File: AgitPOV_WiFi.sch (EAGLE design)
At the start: 42 parts

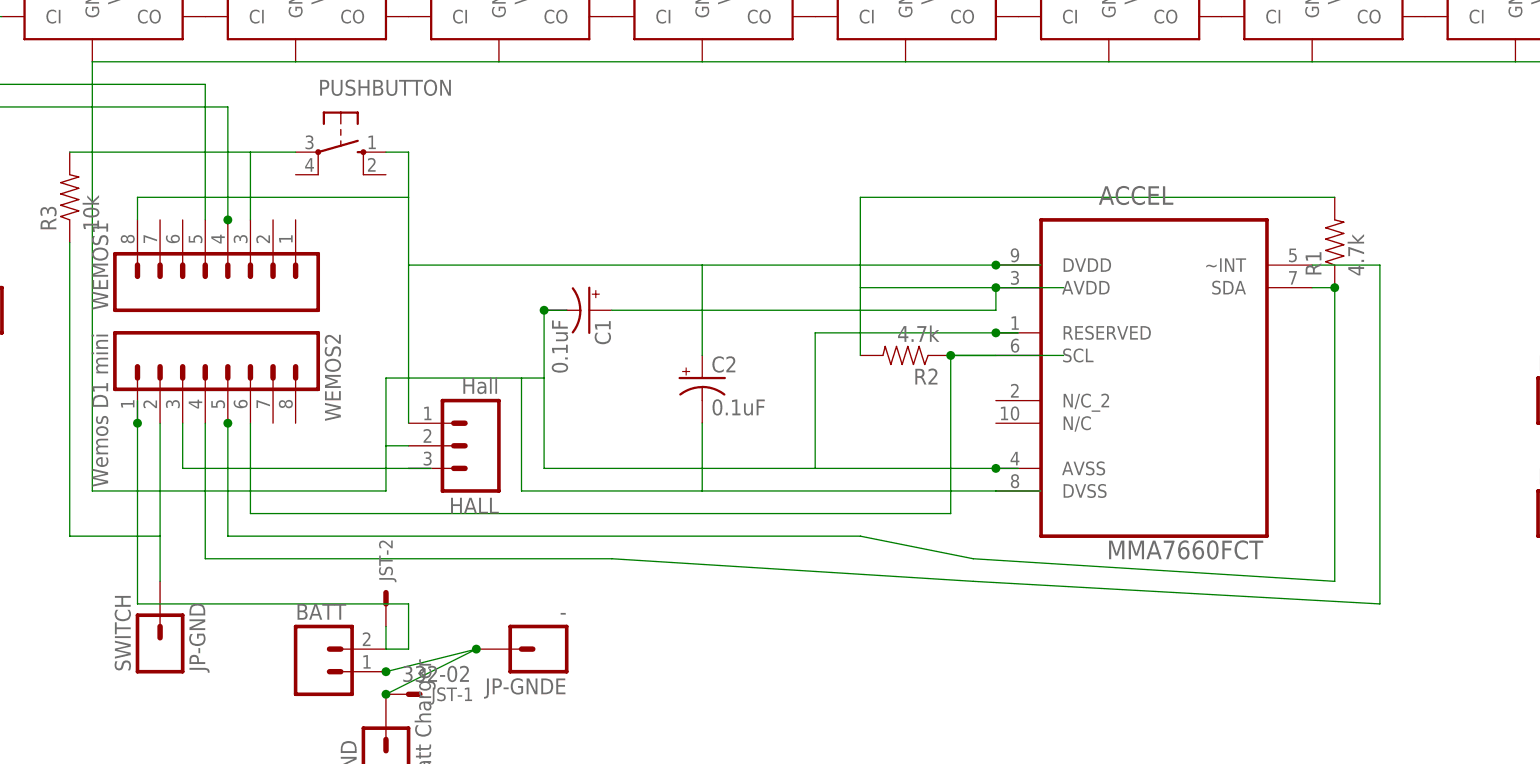
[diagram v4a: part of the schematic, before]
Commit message: Changed the interrupt pin from D3 to D7
D3 (and D4) when pulled to GND will prevent the Wemos from booting :/.
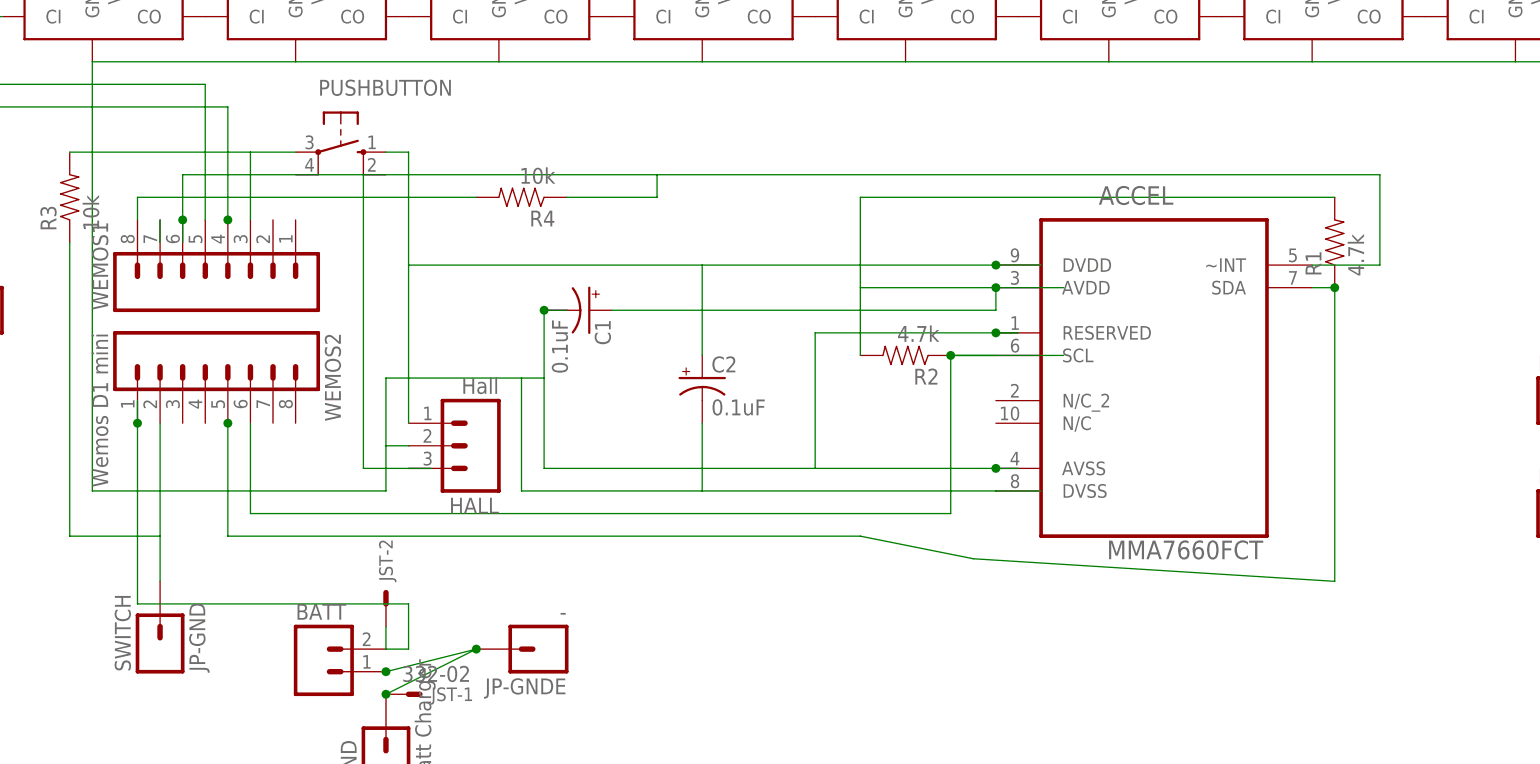
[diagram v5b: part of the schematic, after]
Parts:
- added R4: 10k, SparkFun-Resistors:RESISTOR1206
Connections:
- net N$5 renamed SCL
- net N$65 renamed SDA
- removed net N$67: ACCEL.~INT, WEMOS2.4
- new net INT: ACCEL.~INT, HALL.3, R4.1, WEMOS1.6
- net +3.3V: now also R4.2
- net N$1: now also WEMOS1.7; no longer HALL.3, WEMOS2.3
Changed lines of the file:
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@@
 <part name="R3" library="SparkFun-Resistors" deviceset="RESISTOR" device="1206" value="10k"/>
 <part name="C2" library="SparkFun-Capacitors" deviceset="10UF-16V-10%(TANT)" device="" value="0.1uF"/>
+<part name="R4" library="SparkFun-Resistors" deviceset="RESISTOR" device="1206" value="10k"/>
 </parts>
 <sheets>
@@
 <instance part="R3" gate="G$1" x="25.4" y="60.96" rot="R90"/>
 <instance part="C2" gate="G$1" x="96.52" y="40.64"/>
+<instance part="R4" gate="G$1" x="76.2" y="60.96" rot="R180"/>
 </instances>
 <busses>
@@
 <wire x1="96.52" y1="43.18" x2="96.52" y2="53.34" width="0.1524" layer="91"/>
 <pinref part="C2" gate="G$1" pin="+"/>
+<wire x1="63.5" y1="60.96" x2="71.12" y2="60.96" width="0.1524" layer="91"/>
+<pinref part="R4" gate="G$1" pin="2"/>
 </segment>
 </net>
@@
 </segment>
 </net>
-<net name="N$1" class="0">
-<segment>
-<pinref part="HALL" gate="G$1" pin="3"/>
-<wire x1="63.5" y1="30.48" x2="66.04" y2="30.48" width="0.1524" layer="91"/>
-<wire x1="63.5" y1="30.48" x2="38.1" y2="30.48" width="0.1524" layer="91"/>
-<wire x1="38.1" y1="30.48" x2="38.1" y2="35.56" width="0.1524" layer="91"/>
-<pinref part="WEMOS2" gate="G$1" pin="3"/>
-</segment>
-</net>
-<net name="N$5" class="0">
+<net name="SCL" class="0">
 <segment>
 <wire x1="137.16" y1="43.18" x2="124.46" y2="43.18" width="0.1524" layer="91"/>
@@
 </segment>
 </net>
-<net name="N$65" class="0">
+<net name="SDA" class="0">
 <segment>
 <wire x1="43.18" y1="35.56" x2="43.18" y2="22.86" width="0.1524" layer="91"/>
@@
 </segment>
 </net>
-<net name="N$67" class="0">
+<net name="INT" class="0">
 <segment>
 <wire x1="165.1" y1="53.34" x2="172.72" y2="53.34" width="0.1524" layer="91"/>
-<wire x1="172.72" y1="53.34" x2="172.72" y2="15.24" width="0.1524" layer="91"/>
-<wire x1="172.72" y1="15.24" x2="127" y2="17.78" width="0.1524" layer="91"/>
-<wire x1="127" y1="17.78" x2="86.36" y2="20.32" width="0.1524" layer="91"/>
-<wire x1="86.36" y1="20.32" x2="40.64" y2="20.32" width="0.1524" layer="91"/>
-<wire x1="40.64" y1="20.32" x2="40.64" y2="35.56" width="0.1524" layer="91"/>
-<pinref part="WEMOS2" gate="G$1" pin="4"/>
 <pinref part="ACCEL" gate="A" pin="~INT"/>
+<wire x1="38.1" y1="63.5" x2="58.42" y2="63.5" width="0.1524" layer="91"/>
+<wire x1="58.42" y1="63.5" x2="91.44" y2="63.5" width="0.1524" layer="91"/>
+<wire x1="91.44" y1="63.5" x2="172.72" y2="63.5" width="0.1524" layer="91"/>
+<wire x1="172.72" y1="63.5" x2="172.72" y2="53.34" width="0.1524" layer="91"/>
+<pinref part="HALL" gate="G$1" pin="3"/>
+<wire x1="63.5" y1="30.48" x2="66.04" y2="30.48" width="0.1524" layer="91"/>
+<wire x1="63.5" y1="30.48" x2="58.42" y2="30.48" width="0.1524" layer="91"/>
+<wire x1="58.42" y1="30.48" x2="58.42" y2="63.5" width="0.1524" layer="91"/>
+<pinref part="R4" gate="G$1" pin="1"/>
+<wire x1="81.28" y1="60.96" x2="91.44" y2="60.96" width="0.1524" layer="91"/>
+<wire x1="91.44" y1="60.96" x2="91.44" y2="63.5" width="0.1524" layer="91"/>
+<wire x1="38.1" y1="63.5" x2="38.1" y2="58.42" width="0.1524" layer="91"/>
+<pinref part="WEMOS1" gate="G$1" pin="6"/>
+<wire x1="38.1" y1="58.42" x2="38.1" y2="55.88" width="0.1524" layer="91"/>
+<junction x="38.1" y="58.42"/>
 </segment>
 </net>
@@
 </segment>
 </net>
+<net name="N$1" class="0">
+<segment>
+<pinref part="WEMOS1" gate="G$1" pin="7"/>
+<wire x1="35.56" y1="58.42" x2="35.56" y2="55.88" width="0.1524" layer="91"/>
+</segment>
+</net>

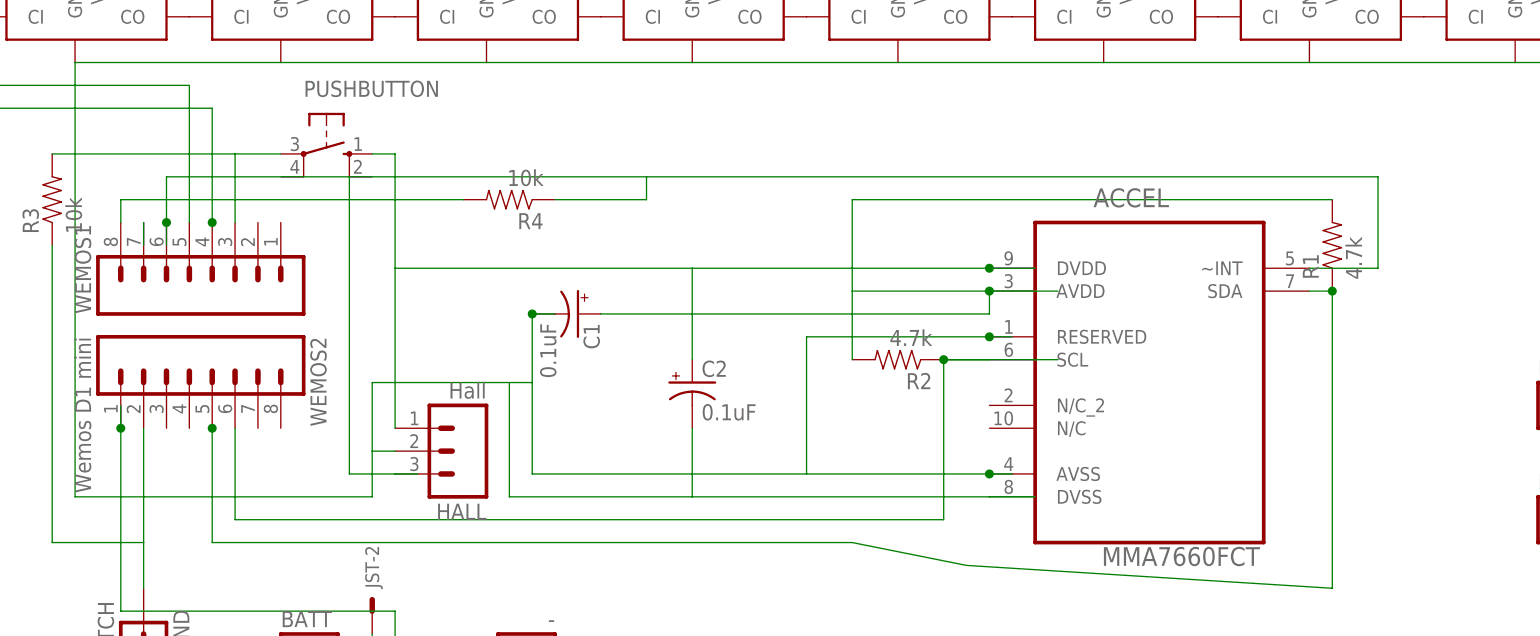
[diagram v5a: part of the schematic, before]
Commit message: Sin interrupt para el ACCEL! De regresar al sensor Hall en D4.
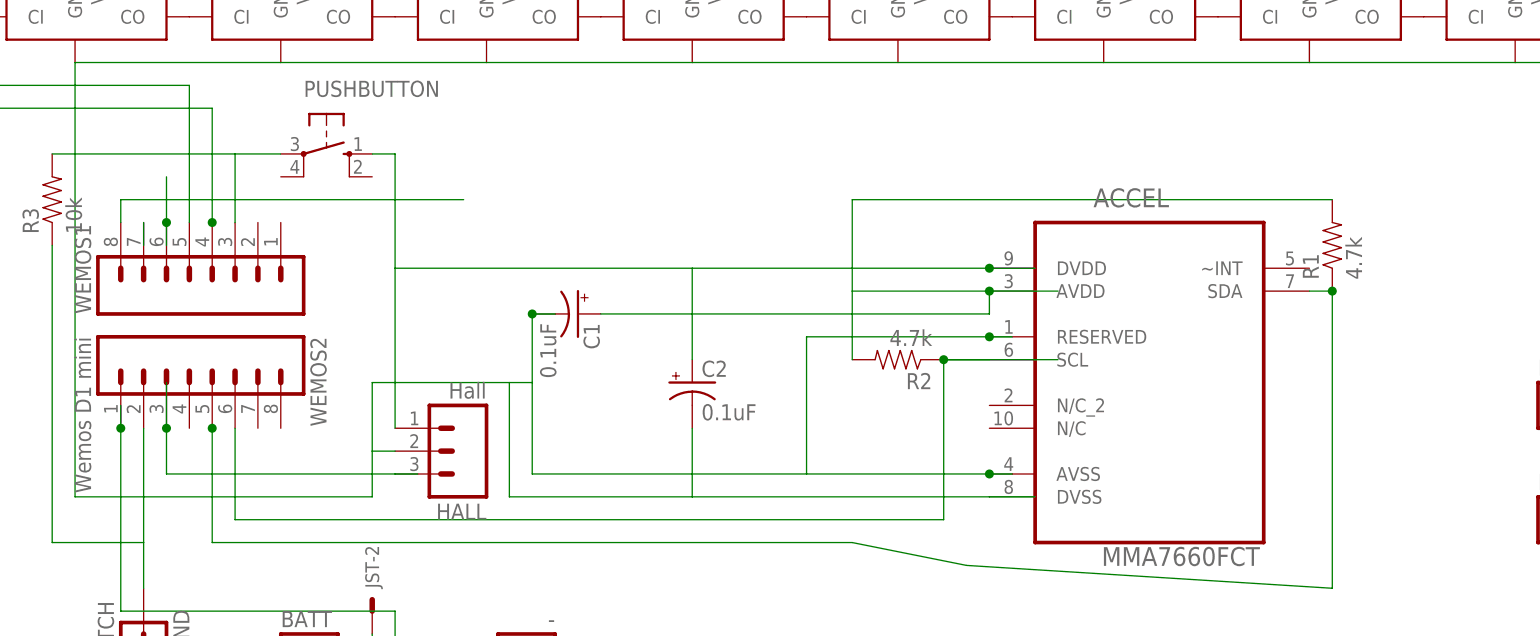
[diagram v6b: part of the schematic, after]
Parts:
- removed R4: 10k, SparkFun-Resistors:RESISTOR1206
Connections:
- removed net INT: ACCEL.~INT, HALL.3, R4.1, WEMOS1.6
- new net N$41: HALL.3, WEMOS2.3
- new net N$65: WEMOS1.6
- net +3.3V: no longer R4.2
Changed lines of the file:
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@@
 <part name="R3" library="SparkFun-Resistors" deviceset="RESISTOR" device="1206" value="10k"/>
 <part name="C2" library="SparkFun-Capacitors" deviceset="10UF-16V-10%(TANT)" device="" value="0.1uF"/>
-<part name="R4" library="SparkFun-Resistors" deviceset="RESISTOR" device="1206" value="10k"/>
 </parts>
 <sheets>
@@
 <instance part="R3" gate="G$1" x="25.4" y="60.96" rot="R90"/>
 <instance part="C2" gate="G$1" x="96.52" y="40.64"/>
-<instance part="R4" gate="G$1" x="76.2" y="60.96" rot="R180"/>
 </instances>
 <busses>
@@
 <pinref part="C2" gate="G$1" pin="+"/>
 <wire x1="63.5" y1="60.96" x2="71.12" y2="60.96" width="0.1524" layer="91"/>
-<pinref part="R4" gate="G$1" pin="2"/>
 </segment>
 </net>
@@
 </segment>
 </net>
-<net name="INT" class="0">
-<segment>
-<wire x1="165.1" y1="53.34" x2="172.72" y2="53.34" width="0.1524" layer="91"/>
-<pinref part="ACCEL" gate="A" pin="~INT"/>
-<wire x1="38.1" y1="63.5" x2="58.42" y2="63.5" width="0.1524" layer="91"/>
-<wire x1="58.42" y1="63.5" x2="91.44" y2="63.5" width="0.1524" layer="91"/>
-<wire x1="91.44" y1="63.5" x2="172.72" y2="63.5" width="0.1524" layer="91"/>
-<wire x1="172.72" y1="63.5" x2="172.72" y2="53.34" width="0.1524" layer="91"/>
-<pinref part="HALL" gate="G$1" pin="3"/>
-<wire x1="63.5" y1="30.48" x2="66.04" y2="30.48" width="0.1524" layer="91"/>
-<wire x1="63.5" y1="30.48" x2="58.42" y2="30.48" width="0.1524" layer="91"/>
-<wire x1="58.42" y1="30.48" x2="58.42" y2="63.5" width="0.1524" layer="91"/>
-<pinref part="R4" gate="G$1" pin="1"/>
-<wire x1="81.28" y1="60.96" x2="91.44" y2="60.96" width="0.1524" layer="91"/>
-<wire x1="91.44" y1="60.96" x2="91.44" y2="63.5" width="0.1524" layer="91"/>
-<wire x1="38.1" y1="63.5" x2="38.1" y2="58.42" width="0.1524" layer="91"/>
-<pinref part="WEMOS1" gate="G$1" pin="6"/>
-<wire x1="38.1" y1="58.42" x2="38.1" y2="55.88" width="0.1524" layer="91"/>
-<junction x="38.1" y="58.42"/>
-</segment>
-</net>
 <net name="PULLDOWN" class="0">
 <segment>
@@
 </segment>
 </net>
+<net name="N$41" class="0">
+<segment>
+<pinref part="HALL" gate="G$1" pin="3"/>
+<wire x1="63.5" y1="30.48" x2="66.04" y2="30.48" width="0.1524" layer="91"/>
+<wire x1="63.5" y1="30.48" x2="38.1" y2="30.48" width="0.1524" layer="91"/>
+<wire x1="38.1" y1="40.64" x2="38.1" y2="35.56" width="0.1524" layer="91"/>
+<pinref part="WEMOS2" gate="G$1" pin="3"/>
+<wire x1="38.1" y1="35.56" x2="38.1" y2="30.48" width="0.1524" layer="91"/>
+<junction x="38.1" y="35.56"/>
+</segment>
+</net>
+<net name="N$65" class="0">
+<segment>
+<wire x1="38.1" y1="63.5" x2="38.1" y2="58.42" width="0.1524" layer="91"/>
+<pinref part="WEMOS1" gate="G$1" pin="6"/>
+<junction x="38.1" y="58.42"/>
+<wire x1="38.1" y1="58.42" x2="38.1" y2="55.88" width="0.1524" layer="91"/>
+</segment>
+</net>

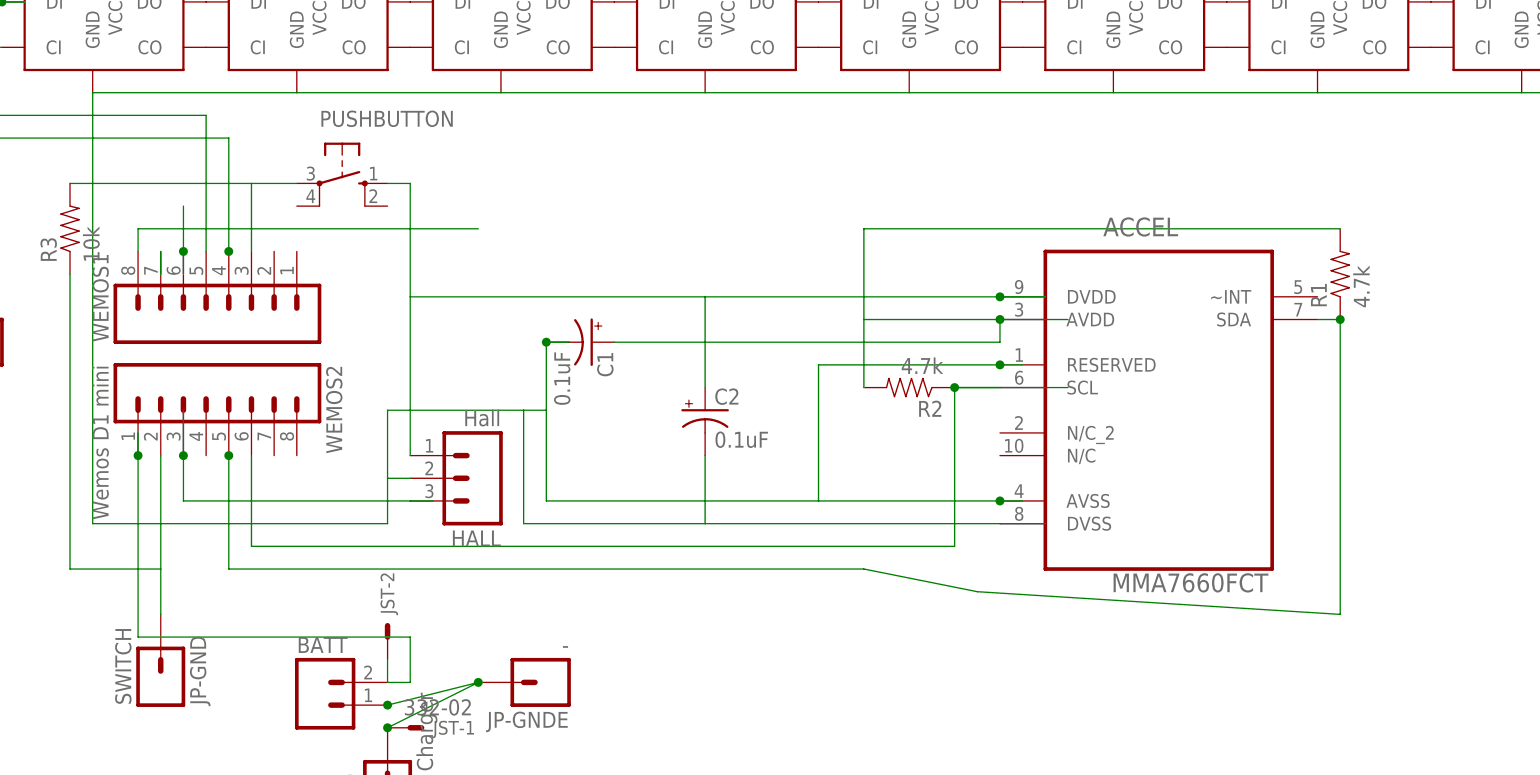
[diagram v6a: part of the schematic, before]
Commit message: Swapped the MMA7660 for the MMA8452Q
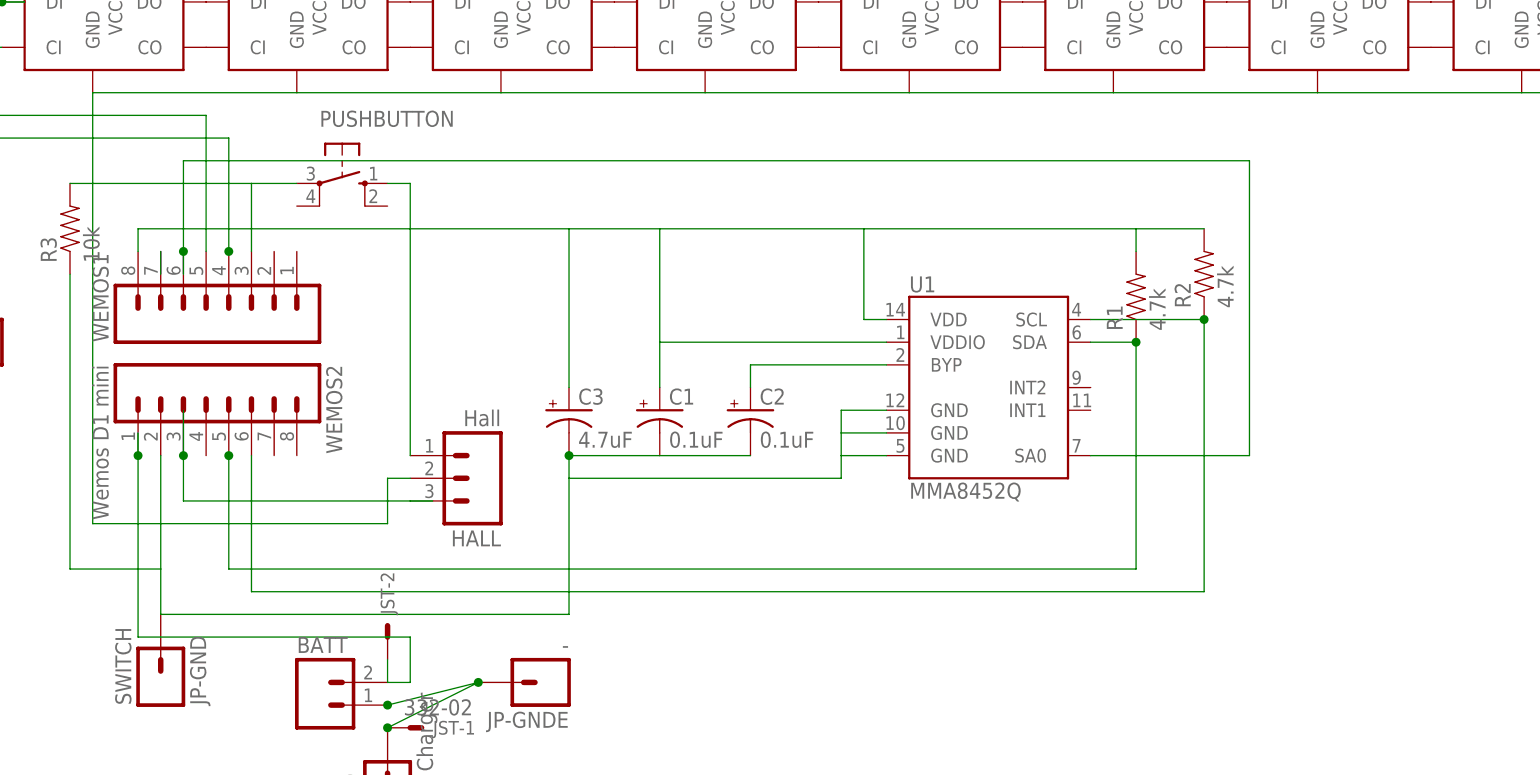
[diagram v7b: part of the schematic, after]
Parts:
- removed ACCEL: MMA7660FCT, Freescale_By_element14_Batch_1:MMA7660FCT
- added C3: 4.7uF, SparkFun-Capacitors:10UF-16V-10%(TANT)
- added U1: MMA8452Q, SparkFun-Sensors:MMA8452Q
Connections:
- removed net N$65: WEMOS1.6
- new net BYP: C2.+, U1.BYP
- new net SA0: U1.SA0, WEMOS1.6
- net +3.3V: now also C3.+, U1.VDD, U1.VDDIO; no longer ACCEL.AVDD, ACCEL.DVDD, C2.+
- net GND: now also C3.-, U1.GND@0, U1.GND@1, U1.GND@2; no longer ACCEL.AVSS, ACCEL.DVSS, ACCEL.RESERVED
- net SCL: now also U1.SCL; no longer ACCEL.SCL
- net SDA: now also U1.SDA; no longer ACCEL.SDA
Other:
- moved on the sheet: C1, C2, R1, R2
